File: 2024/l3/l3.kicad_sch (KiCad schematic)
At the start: 23 parts, among them J1 Conn_01x04, SW1 SW_SPDT, SW2 SW_SPDT, SW3 SW_SPDT, SW4 SW_SPDT, U4 DEV-15583

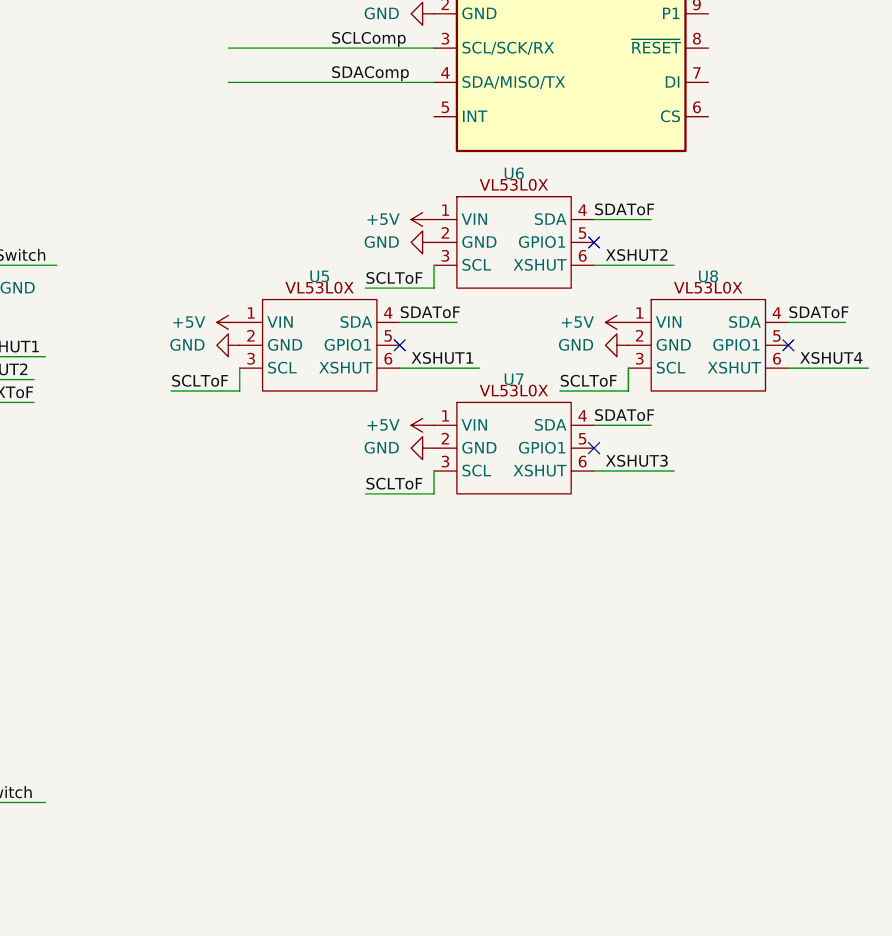
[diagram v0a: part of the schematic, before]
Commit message: Fixed motor driver error
VL53L1X is actual one
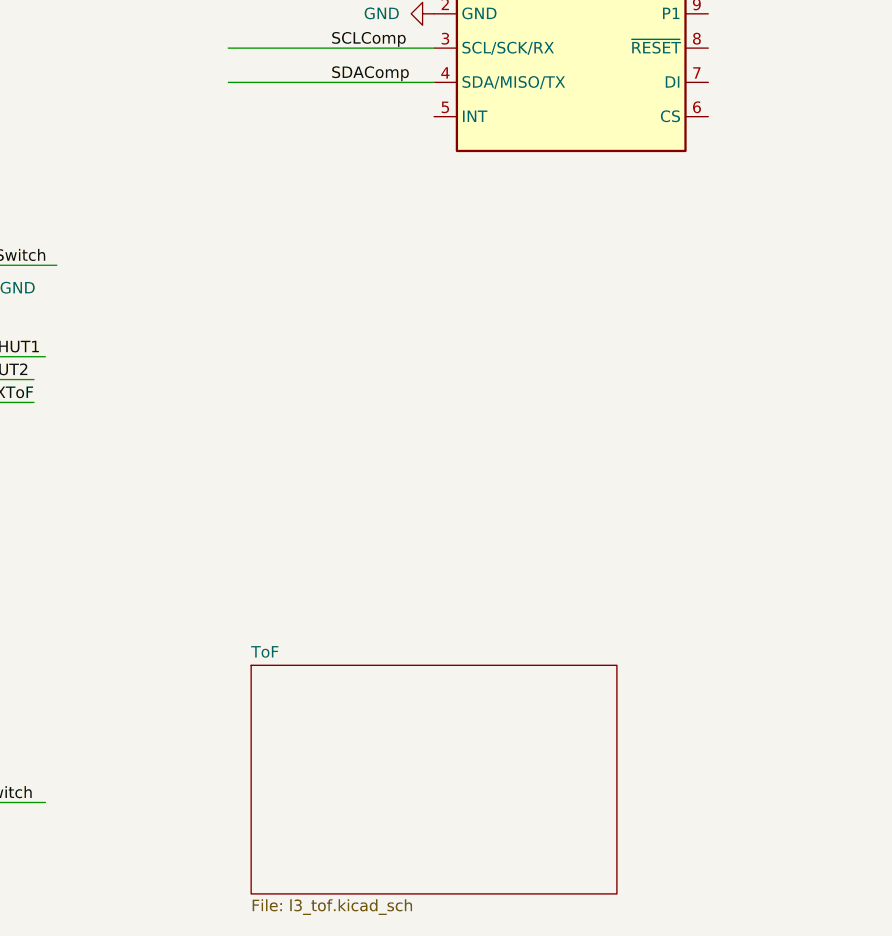
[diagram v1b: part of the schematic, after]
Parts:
- removed U5, U6, U7, U8: ~, Connector_PinHeader_2.54mm:PinHeader_1x06_P2.54mm_Vertical, symbol Sensor_Distance:VL53L0X
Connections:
- no-connect marks 22 -> 18
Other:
- added sheet ToF (l3_tof.kicad_sch)

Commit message: 16/8 final
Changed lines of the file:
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@@
 	)
 	(sheet
-		(at 187.96 137.16)
+		(at 198.12 114.3)
 		(size 40.64 25.4)
 		(fields_autoplaced yes)
@@
 		)
 		(property "Sheetname" "ToF"
-			(at 187.96 136.4484 0)
+			(at 198.12 113.5884 0)
 			(effects
 				(font
@@
 		)
 		(property "Sheetfile" "l3_tof.kicad_sch"
-			(at 187.96 163.1446 0)
+			(at 198.12 140.2846 0)
 			(effects
 				(font

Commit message: final 0.9
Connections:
- no-connect marks 18 -> 26
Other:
- moved on the sheet: R1, R2

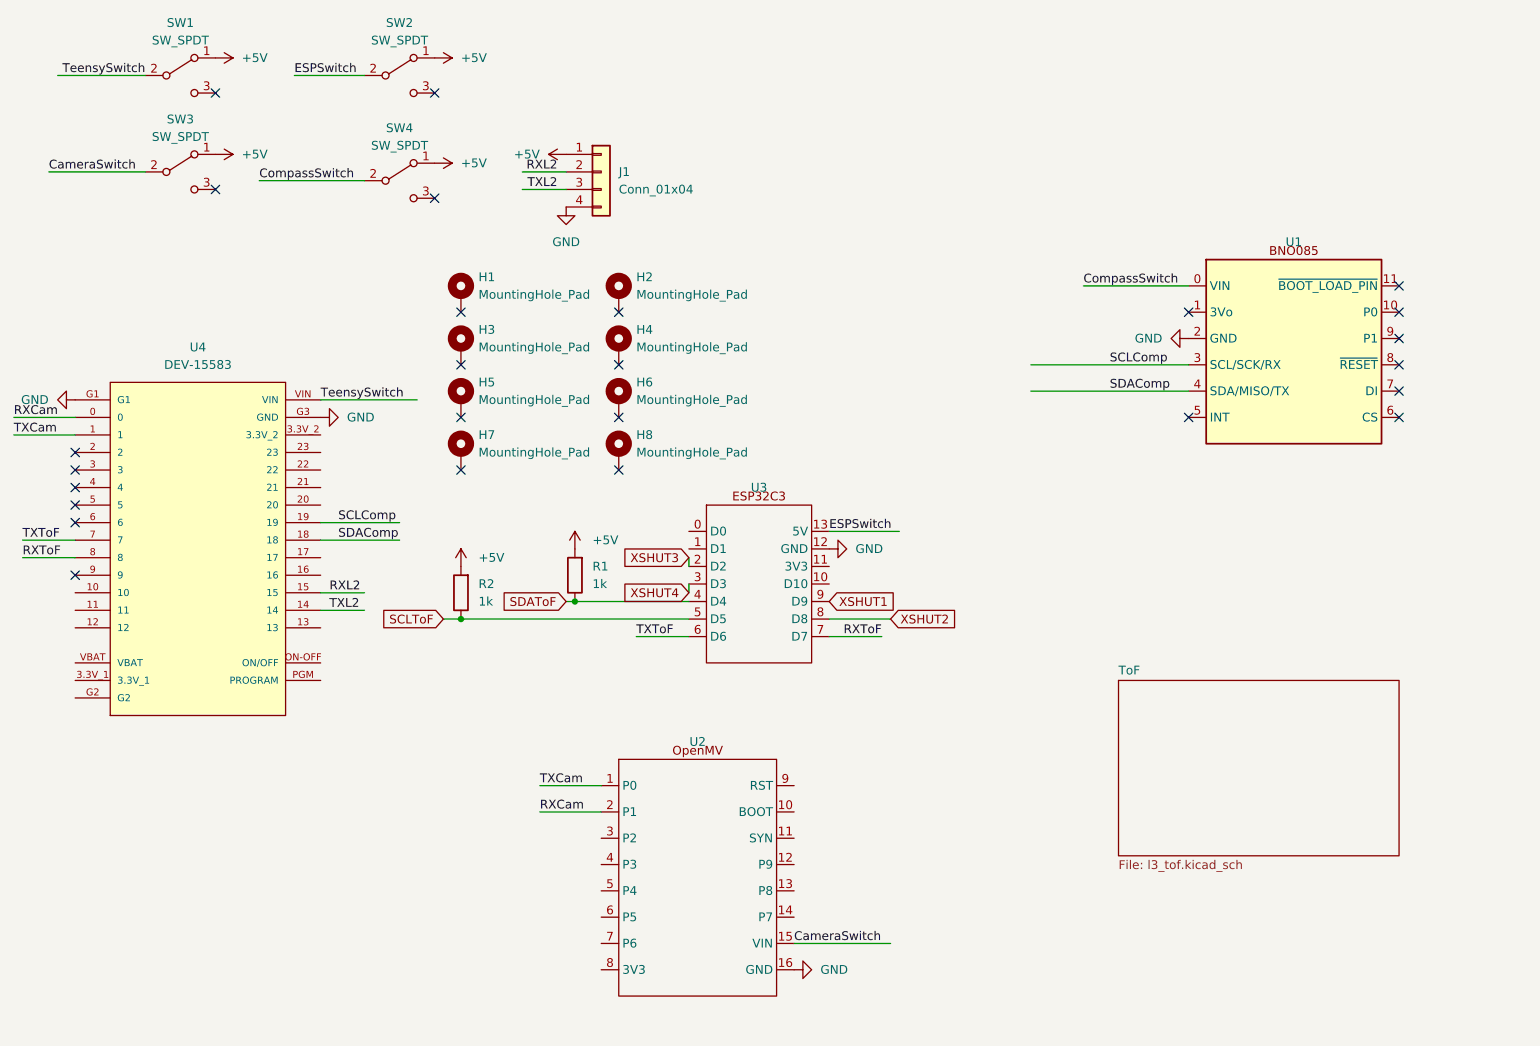
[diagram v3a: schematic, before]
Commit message: tf luna
gerber created for l1 and l2
l3 changed the tof from vl53l1x to tf luna
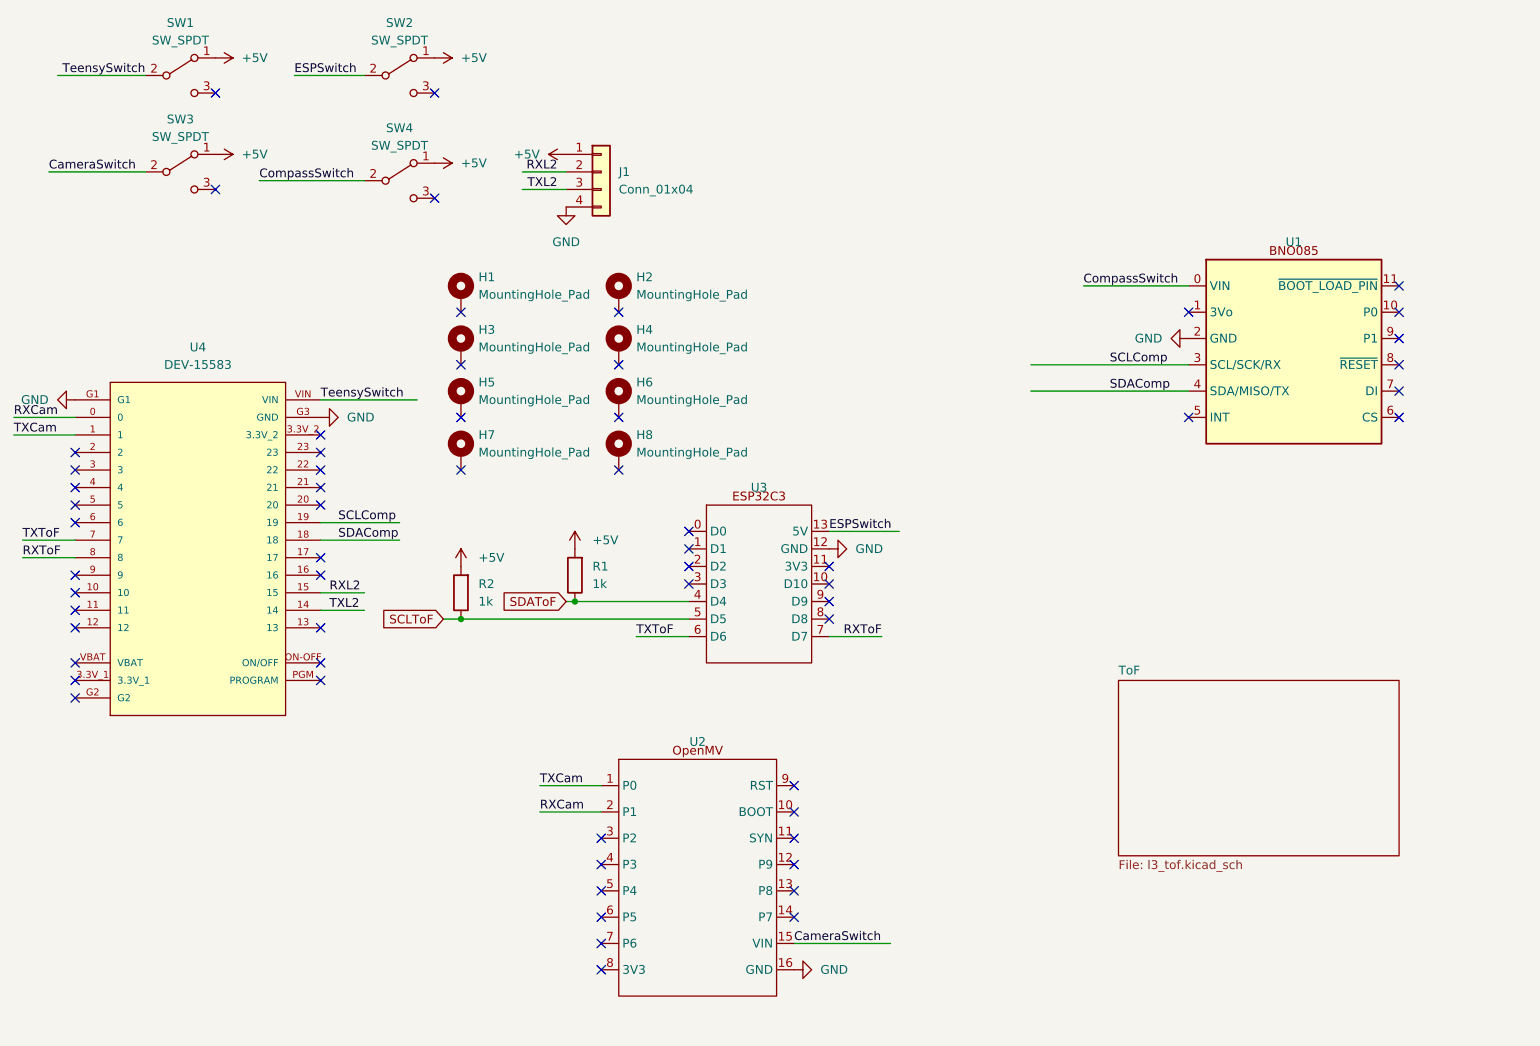
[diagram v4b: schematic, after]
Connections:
- net XSHUT1: no longer names the net of U3.9 (D9)
- net XSHUT2: no longer names the net of U3.8 (D8)
- net XSHUT3: no longer names the net of U3.2 (D2)
- net XSHUT4: no longer names the net of U3.3 (D3)
- no-connect marks 26 -> 62
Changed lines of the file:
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@@
+	)
+	(no_connect
+		(at 123.19 137.16)
+	)
+	(no_connect
+		(at 46.99 116.84)
 	)
 	(no_connect
@@
 	)
 	(no_connect
+		(at 151.13 140.97)
+	)
+	(no_connect
+		(at 151.13 148.59)
+	)
+	(no_connect
+		(at 156.21 100.33)
+	)
+	(no_connect
+		(at 123.19 140.97)
+	)
+	(no_connect
+		(at 82.55 96.52)
+	)
+	(no_connect
+		(at 135.89 97.79)
+	)
+	(no_connect
+		(at 151.13 133.35)
+	)
+	(no_connect
 		(at 46.99 91.44)
 	)
 	(no_connect
+		(at 82.55 111.76)
+	)
+	(no_connect
+		(at 156.21 97.79)
+	)
+	(no_connect
 		(at 46.99 99.06)
 	)
@@
 	)
 	(no_connect
+		(at 135.89 100.33)
+	)
+	(no_connect
+		(at 151.13 129.54)
+	)
+	(no_connect
+		(at 123.19 152.4)
+	)
+	(no_connect
 		(at 238.76 64.77)
 	)
@@
 	)
 	(no_connect
+		(at 82.55 88.9)
+	)
+	(no_connect
+		(at 135.89 92.71)
+	)
+	(no_connect
 		(at 67.31 43.18)
 	)
 	(no_connect
+		(at 46.99 106.68)
+	)
+	(no_connect
+		(at 46.99 114.3)
+	)
+	(no_connect
 		(at 102.87 76.2)
 	)
 	(no_connect
+		(at 156.21 102.87)
+	)
+	(no_connect
+		(at 82.55 99.06)
+	)
+	(no_connect
+		(at 82.55 106.68)
+	)
+	(no_connect
 		(at 125.73 76.2)
 	)
 	(no_connect
+		(at 82.55 78.74)
+	)
+	(no_connect
 		(at 238.76 57.15)
 	)
@@
 	)
 	(no_connect
+		(at 82.55 81.28)
+	)
+	(no_connect
+		(at 123.19 144.78)
+	)
+	(no_connect
 		(at 238.76 72.39)
 	)
@@
 	)
 	(no_connect
+		(at 82.55 114.3)
+	)
+	(no_connect
+		(at 82.55 83.82)
+	)
+	(no_connect
 		(at 46.99 88.9)
 	)
@@
 	)
 	(no_connect
+		(at 123.19 148.59)
+	)
+	(no_connect
+		(at 156.21 105.41)
+	)
+	(no_connect
 		(at 99.06 29.21)
 	)
 	(no_connect
+		(at 151.13 137.16)
+	)
+	(no_connect
 		(at 46.99 81.28)
 	)
 	(no_connect
+		(at 123.19 156.21)
+	)
+	(no_connect
+		(at 82.55 86.36)
+	)
+	(no_connect
 		(at 67.31 29.21)
 	)
 	(no_connect
+		(at 46.99 101.6)
+	)
+	(no_connect
+		(at 46.99 104.14)
+	)
+	(no_connect
+		(at 151.13 144.78)
+	)
+	(no_connect
 		(at 102.87 68.58)
 	)
+	(no_connect
+		(at 135.89 95.25)
+	)
+	(no_connect
+		(at 46.99 111.76)
+	)
 	(wire
 		(pts
@@
 	(wire
 		(pts
-			(xy 135.89 101.6) (xy 135.89 100.33)
-		)
-		(stroke
-			(width 0)
-			(type default)
-		)
-	)
-	(wire
-		(pts
 			(xy 39.37 93.98) (xy 46.99 93.98)
 		)
@@
 		(pts
 			(xy 128.27 107.95) (xy 135.89 107.95)
-		)
-		(stroke
-			(width 0)
-			(type default)
-		)
-	)
-	(wire
-		(pts
-			(xy 165.1 105.41) (xy 156.21 105.41)
-		)
-		(stroke
-			(width 0)
-			(type default)
-		)
-	)
-	(wire
-		(pts
-			(xy 135.89 96.52) (xy 135.89 97.79)
 		)
 		(stroke
@@
 			)
 			(justify left bottom)
-		)
-	)
-	(global_label "XSHUT2"
-		(shape input)
-		(at 165.1 105.41 0)
-		(fields_autoplaced yes)
-		(effects
-			(font
-				(size 1.27 1.27)
-			)
-			(justify left)
-		)
-		(property "Intersheetrefs" "${INTERSHEET_REFS}"
-			(at 175.3423 105.41 0)
-			(effects
-				(font
-					(size 1.27 1.27)
-				)
-				(justify left)
-				(hide yes)
-			)
 		)
 	)
@@
 			(effects
 				(font
-					(size 1.27 1.27)
-				)
-				(justify right)
-				(hide yes)
-			)
-		)
-	)
-	(global_label "XSHUT1"
-		(shape input)
-		(at 156.21 102.87 0)
-		(fields_autoplaced yes)
-		(effects
-			(font
-				(size 1.27 1.27)
-			)
-			(justify left)
-		)
-		(property "Intersheetrefs" "${INTERSHEET_REFS}"
-			(at 166.4523 102.87 0)
-			(effects
-				(font
-					(size 1.27 1.27)
-				)
-				(justify left)
-				(hide yes)
-			)
-		)
-	)
-	(global_label "XSHUT4"
-		(shape input)
-		(at 135.89 101.6 180)
-		(fields_autoplaced yes)
-		(effects
-			(font
-				(size 1.27 1.27)
-			)
-			(justify right)
-		)
-		(property "Intersheetrefs" "${INTERSHEET_REFS}"
-			(at 125.6477 101.6 0)
-			(effects
-				(font
-					(size 1.27 1.27)
-				)
-				(justify right)
-				(hide yes)
-			)
-		)
-	)
-	(global_label "XSHUT3"
-		(shape input)
-		(at 135.89 96.52 180)
-		(fields_autoplaced yes)
-		(effects
-			(font
-				(size 1.27 1.27)
-			)
-			(justify right)
-		)
-		(property "Intersheetrefs" "${INTERSHEET_REFS}"
-			(at 125.6477 96.52 0)
-			(effects
-				(font
